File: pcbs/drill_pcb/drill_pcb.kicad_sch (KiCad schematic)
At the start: 12 parts, among them SW101 RPi reset, U101 TXS0108EPW, U102 Pico

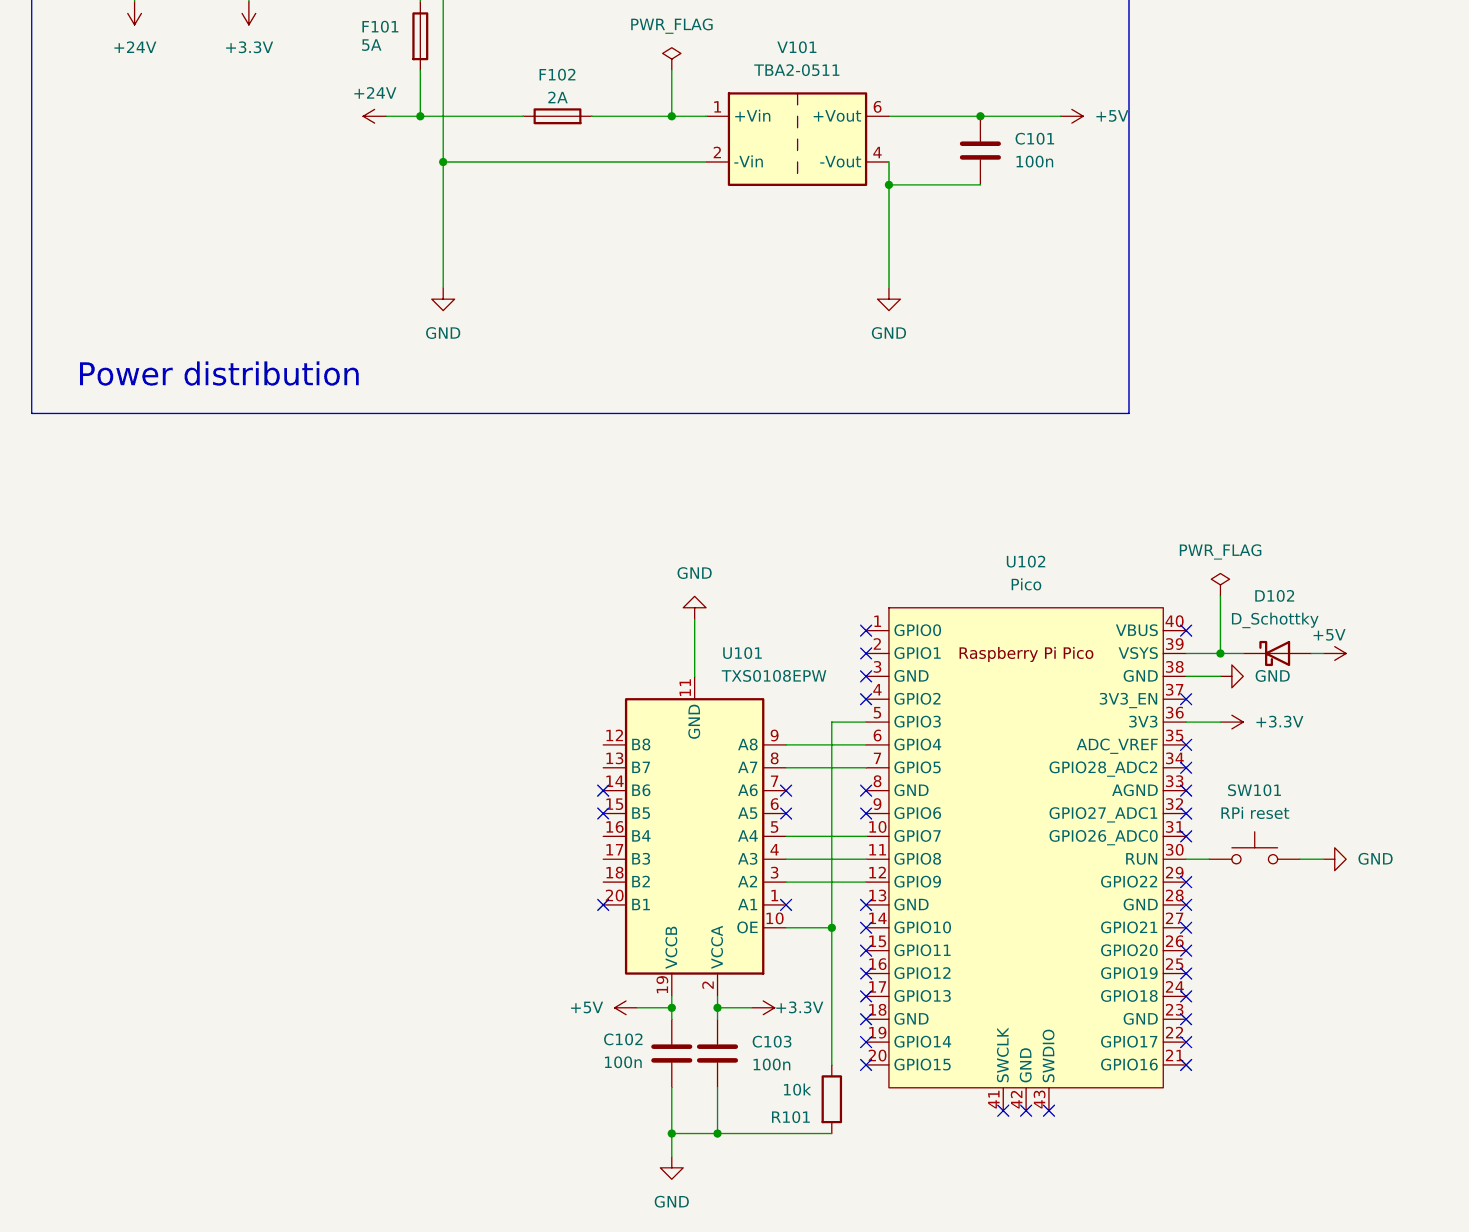
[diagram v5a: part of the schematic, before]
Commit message: pcb changes, added ESP library
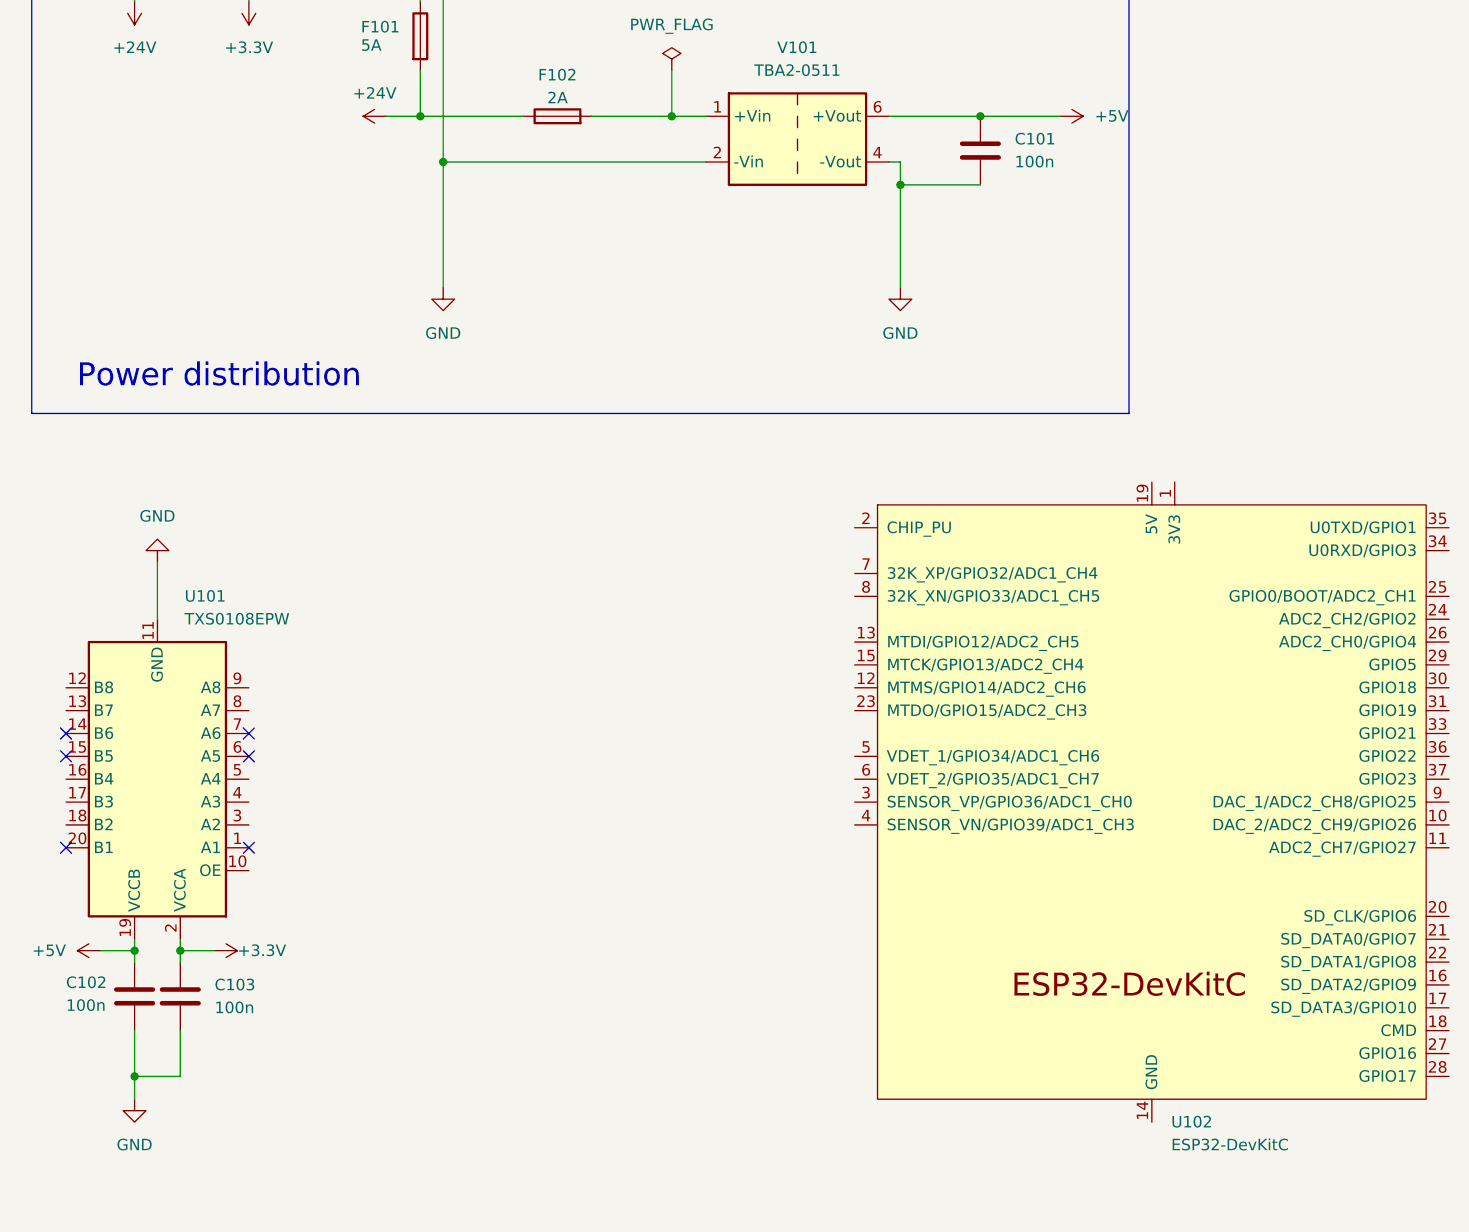
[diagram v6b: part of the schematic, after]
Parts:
- removed D102: D_Schottky, Diode_SMD:D_SOD-123, symbol Device:D_Schottky
- removed R101: 10k, Resistor_SMD:R_1206_3216Metric_Pad1.30x1.75mm_HandSolder, symbol Device:R
- removed SW101: RPi reset, Button_Switch_THT:SW_PUSH_6mm_H5mm, symbol Switch:SW_Push
- removed U102: Pico, drill_RP-Pico Libraries:RPi_Pico_SMD_TH, symbol MCU_RaspberryPi_and_Boards:Pico
- added U102: ESP32-DevKitC, PCM_Espressif:ESP32-DevKitC, symbol drill_Espressif:ESP32-DevKitC
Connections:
- new net: U102.14 (GND), U102.32 (GND), U102.38 (GND)
- no-connect marks 39 -> 6
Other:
- moved on the sheet: C102, C103, U101

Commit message: PCB changes
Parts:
- added J1: WEIGHT SENSOR, Connector_JST:JST_XH_B7B-XH-A_1x07_P2.50mm_Vertical, symbol Connector:Screw_Terminal_01x07
- added J10: DC MOTOR UART, drill_T-DEAN:DEANS, symbol Connector:Screw_Terminal_01x02
- added J2: DC MOTOR 24 V, drill_T-DEAN:DEANS, symbol Connector:Screw_Terminal_01x02
- added J3: LIMIT SENSOR TOP, Connector_JST:JST_XH_B3B-XH-A_1x03_P2.50mm_Vertical, symbol Connector:Screw_Terminal_01x03
- added J4: LIMIT SENSOR BOTTOM, Connector_JST:JST_XH_B3B-XH-A_1x03_P2.50mm_Vertical, symbol Connector:Screw_Terminal_01x03
- added J5: ENCODER VERTICAL DRIVE, Connector_JST:JST_XH_B4B-XH-A_1x04_P2.50mm_Vertical, symbol Connector:Screw_Terminal_01x04
- added J6: ENCODER STORAGE, Connector_JST:JST_XH_B4B-XH-A_1x04_P2.50mm_Vertical, symbol Connector:Screw_Terminal_01x04
- added J7: HEIGHT SENSOR, Connector_JST:JST_XH_B4B-XH-A_1x04_P2.50mm_Vertical, symbol Connector:Screw_Terminal_01x04
- added J8: STEPPER VERTICAL DRIVE, Connector_JST:JST_XH_B4B-XH-A_1x04_P2.50mm_Vertical, symbol Connector:Screw_Terminal_01x04
- added J9: STEPPER STORAGE, Connector_JST:JST_XH_B4B-XH-A_1x04_P2.50mm_Vertical, symbol Connector:Screw_Terminal_01x04
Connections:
- net +24V: now also J2.1 (Pin_1)
- net +3.3V: now also J1.2 (Pin_2), J3.1 (Pin_1), J4.1 (Pin_1), J5.2 (Pin_2), J6.2 (Pin_2), J7.2 (Pin_2)
- net +5V: now also J1.1 (Pin_1)
- net GND: now also U102.14 (GND), U102.32 (GND), U102.38 (GND), J1.7 (Pin_7), J2.2 (Pin_2), J3.3 (Pin_3), J4.3 (Pin_3), J5.3 (Pin_3), J6.3 (Pin_3), J7.3 (Pin_3)
- new net ADC_DRDY: J1.5 (Pin_5)
- new net ADC_RST: J1.6 (Pin_6)
- new net LIMIT_SENSOR_BOTTOM: J4.2 (Pin_2)
- new net LIMIT_SENSOR_TOP: J3.2 (Pin_2)
- new net RX2: J10.2 (Pin_2)
- new net SCL1: J1.3 (Pin_3), J5.4 (Pin_4), J6.4 (Pin_4), J7.4 (Pin_4)
- new net SDA1: J1.4 (Pin_4), J5.1 (Pin_1), J6.1 (Pin_1), J7.1 (Pin_1)
- new net TX2: J10.1 (Pin_1)
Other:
- moved on the sheet: U102

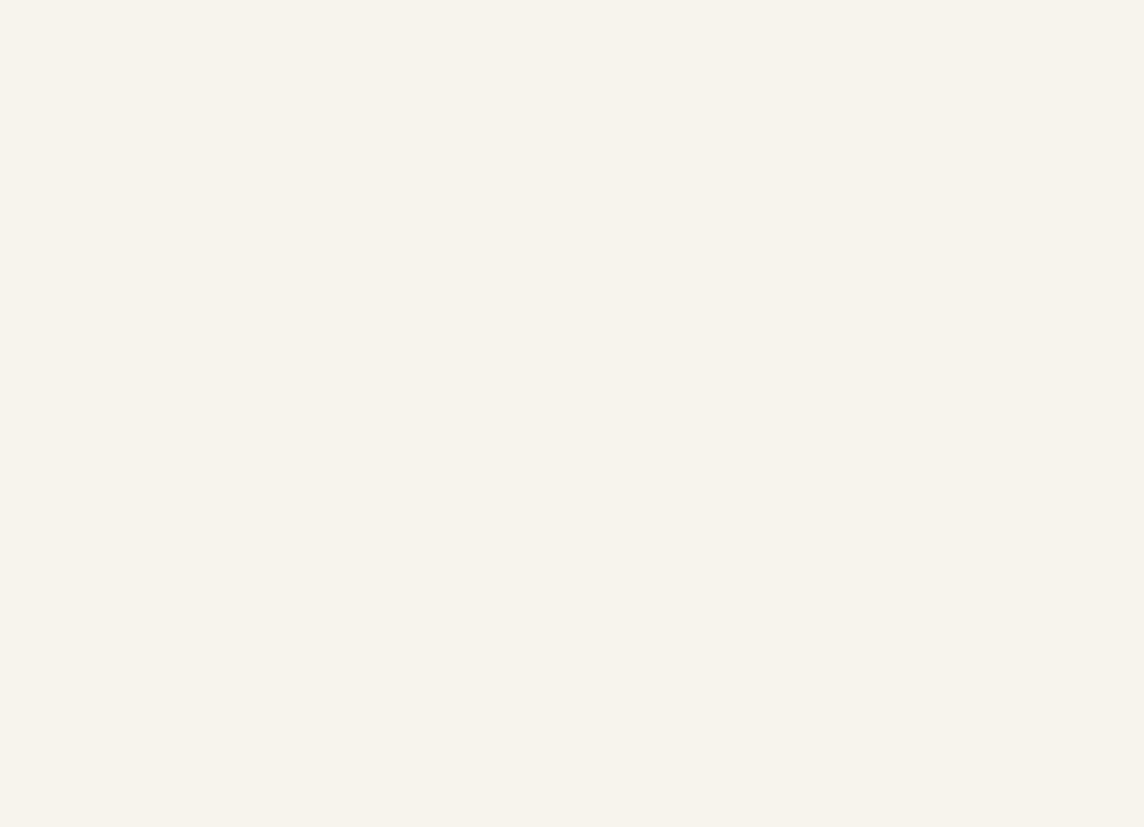
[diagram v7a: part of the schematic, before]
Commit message: pridany drivery a ldo (nehotove)
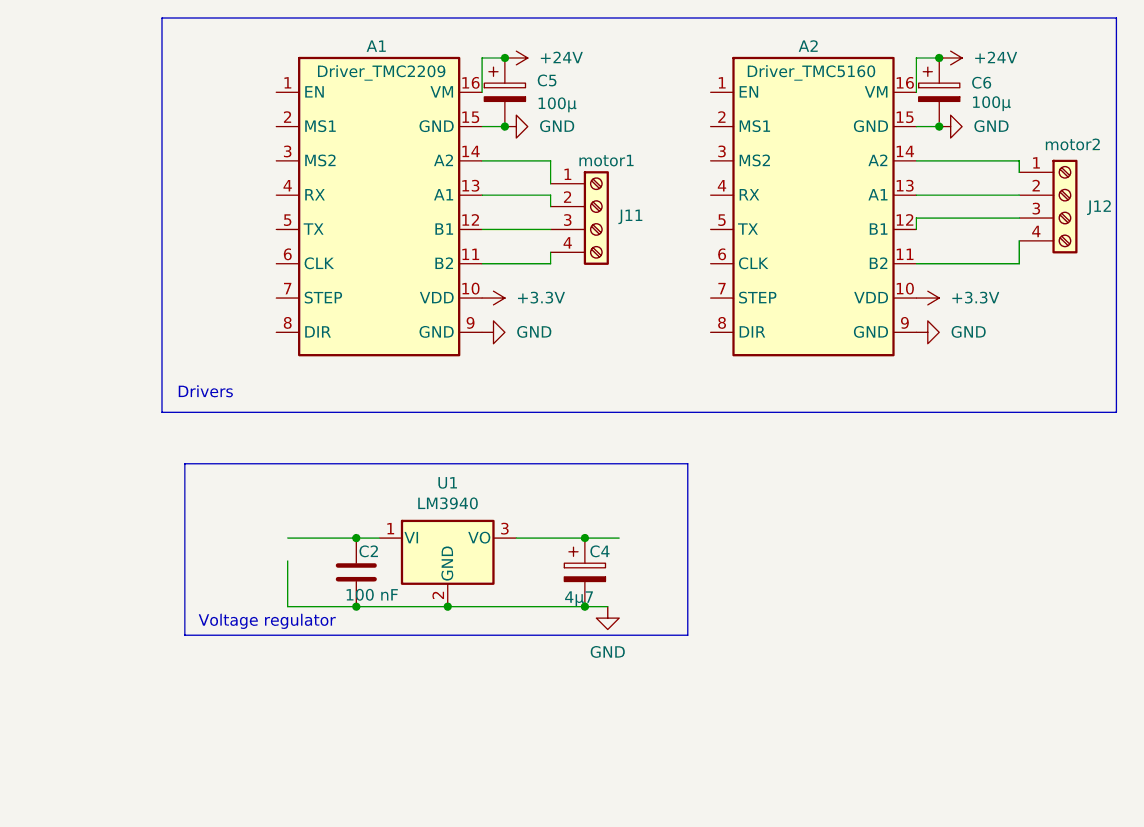
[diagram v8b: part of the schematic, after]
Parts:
- added A1: Driver_TMC2209, Module:Pololu_Breakout-16_15.2x20.3mm, symbol mujDriver:mujDriver2
- added A2: Driver_TMC5160, Module:Pololu_Breakout-16_15.2x20.3mm, symbol mujDriver:mujDriver2
- added C2: 100 nF, Capacitor_THT:C_Disc_D4.3mm_W1.9mm_P5.00mm, symbol Device:C
- added C4: 4μ7, Capacitor_THT:CP_Radial_D5.0mm_P2.50mm, symbol Device:C_Polarized
- added C5, C6: 100μ, Capacitor_THT:CP_Radial_D8.0mm_P3.50mm, symbol Device:C_Polarized
- added J11: motor1, Connector_JST:JST_XH_B4B-XH-A_1x04_P2.50mm_Vertical, symbol Connector:Screw_Terminal_01x04
- added J12: motor2, Connector_JST:JST_XH_B4B-XH-A_1x04_P2.50mm_Vertical, symbol Connector:Screw_Terminal_01x04
- added U1: LM3940, Package_TO_SOT_THT:TO-220-3_Vertical, symbol Regulator_Linear:LM7805_TO220
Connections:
- net +24V: now also A1.16 (VM), A2.16 (VM), C5.1, C6.1
- net +3.3V: now also A1.10 (VDD), A2.10 (VDD)
- net GND: now also A1.15 (GND), A1.9 (GND), A2.15 (GND), A2.9 (GND), C2.2, C4.2, C5.2, C6.2, U1.2 (GND)
- new net: C2.1, U1.1 (VI)
- new net: C4.1, U1.3 (VO)
- new net: A1.14 (A2), J11.1 (Pin_1)
- new net: A1.13 (A1), J11.2 (Pin_2)
- new net: A1.12 (B1), J11.3 (Pin_3)
- new net: A1.11 (B2), J11.4 (Pin_4)
- new net: A2.11 (B2), J12.4 (Pin_4)
- new net: A2.12 (B1), J12.3 (Pin_3)
- new net: A2.13 (A1), J12.2 (Pin_2)
- new net: A2.14 (A2), J12.1 (Pin_1)
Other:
- note added: "Drivers"
- note added: "Voltage regulator"
